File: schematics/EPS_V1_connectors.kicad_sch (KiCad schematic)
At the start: 14 parts, among them J1 Conn_01x19, J2 Conn_01x25, J3 Conn_01x9, J4 Conn_01x02, SW1 SWITCH, SW2 SWITCH, SW3 SWITCH

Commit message: Expose unregulated battery voltage for burn wire
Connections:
- net +12V: no longer J2.2 (Pin_2)
- net CHG_OUT: now also J2.2 (Pin_2)
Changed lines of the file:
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@@
 	)
 	(junction
-		(at 82.55 111.76)
-		(diameter 0)
-		(color 0 0 0 0)
-	)
-	(junction
 		(at 82.55 55.88)
 		(diameter 0)
@@
 	(wire
 		(pts
-			(xy 82.55 111.76) (xy 87.63 111.76)
-		)
-		(stroke
-			(width 0)
-			(type default)
-		)
-	)
-	(wire
-		(pts
 			(xy 82.55 58.42) (xy 82.55 60.96)
 		)
@@
 	(wire
 		(pts
-			(xy 82.55 111.76) (xy 82.55 114.3)
-		)
-		(stroke
-			(width 0)
-			(type default)
-		)
-	)
-	(wire
-		(pts
 			(xy 46.99 92.71) (xy 44.45 92.71)
 		)
@@
 	(wire
 		(pts
+			(xy 82.55 114.3) (xy 95.25 114.3)
+		)
+		(stroke
+			(width 0)
+			(type default)
+		)
+	)
+	(wire
+		(pts
 			(xy 46.99 97.79) (xy 44.45 97.79)
 		)
@@
 		)
 	)
+	(global_label "CHG_OUT"
+		(shape passive)
+		(at 82.55 111.76 0)
+		(fields_autoplaced yes)
+		(effects
+			(font
+				(size 1.27 1.27)
+			)
+			(justify left)
+		)
+		(property "Intersheetrefs" "${INTERSHEET_REFS}"
+			(at 92.8906 111.76 0)
+			(hide yes)
+			(show_name no)
+			(do_not_autoplace no)
+			(effects
+				(font
+					(size 1.27 1.27)
+				)
+				(justify left)
+			)
+		)
+	)
 	(global_label "I2C3_SDA"
 		(shape bidirectional)
@@
 	)
 	(symbol
-		(lib_id "power:+12V")
-		(at 87.63 111.76 0)
+		(lib_id "Device:D_Schottky")
+		(at 195.58 64.77 180)
 		(unit 1)
 		(body_style 1)
@@
 		(dnp no)
 		(fields_autoplaced yes)
-		(property "Reference" "#PWR016"
-			(at 87.63 115.57 0)
-			(hide yes)
+		(property "Reference" "D1"
+			(at 195.8975 58.42 0)
 			(show_name no)
 			(do_not_autoplace no)
@@
 			)
 		)
-		(property "Value" "+12V"
-			(at 87.63 106.68 0)
+		(property "Value" "D_Schottky"
+			(at 195.8975 60.96 0)
 			(show_name no)
 			(do_not_autoplace no)
@@
 			)
 		)
-		(property "Footprint" ""
-			(at 87.63 111.76 0)
+		(property "Footprint" "Diode_SMD:D_SOD-128"
+			(at 195.58 64.77 0)
 			(hide yes)
 			(show_name no)
@@
 		)
 		(property "Datasheet" ""
-			(at 87.63 111.76 0)
+			(at 195.58 64.77 0)
 			(hide yes)
 			(show_name no)
@@
 			)
 		)
-		(property "Description" "Power symbol creates a global label with name \"+12V\""
-			(at 87.63 111.76 0)
+		(property "Description" "Schottky diode"
+			(at 195.58 64.77 0)
 			(hide yes)
 			(show_name no)
@@
 			)
 		)
+		(property "MPN" "RSX301LAM30TR"
+			(at 195.58 64.77 0)
+			(hide yes)
+			(show_name no)
+			(do_not_autoplace no)
+			(effects
+				(font
+					(size 1.27 1.27)
+				)
+			)
+		)
+		(pin "2"
+		)
 		(pin "1"
 		)
@@
 			(project "EPS_V1"
 				(path "/85157432-5d03-48fa-ab40-27ed3d133f47/dccdebb8-bc98-4226-b239-70e380ba944d"
-					(reference "#PWR016")
+					(reference "D1")
 					(unit 1)
 				)
@@
 	)
 	(symbol
-		(lib_id "Device:D_Schottky")
-		(at 195.58 64.77 180)
+		(lib_id "Device:R_US")
+		(at 142.24 74.93 270)
 		(unit 1)
 		(body_style 1)
@@
 		(in_pos_files yes)
 		(dnp no)
-		(fields_autoplaced yes)
-		(property "Reference" "D1"
-			(at 195.8975 58.42 0)
+		(property "Reference" "R_ALRT1"
+			(at 145.796 72.644 90)
 			(show_name no)
 			(do_not_autoplace no)
@@
 					(size 1.27 1.27)
 				)
+				(justify right)
 			)
 		)
-		(property "Value" "D_Schottky"
-			(at 195.8975 60.96 0)
+		(property "Value" "1k"
+			(at 143.764 70.104 90)
 			(show_name no)
 			(do_not_autoplace no)
@@
 					(size 1.27 1.27)
 				)
+				(justify right)
 			)
 		)
-		(property "Footprint" "Diode_SMD:D_SOD-128"
-			(at 195.58 64.77 0)
+		(property "Footprint" "Resistor_SMD:R_0603_1608Metric"
+			(at 141.986 75.946 90)
 			(hide yes)
 			(show_name no)
@@
 		)
 		(property "Datasheet" ""
-			(at 195.58 64.77 0)
-			(hide yes)
-			(show_name no)
-			(do_not_autoplace no)
-			(effects
-				(font
-					(size 1.27 1.27)
-				)
-			)
-		)
-		(property "Description" "Schottky diode"
-			(at 195.58 64.77 0)
+			(at 142.24 74.93 0)
 			(hide yes)
 			(show_name no)
@@
 			)
 		)
-		(property "MPN" "RSX301LAM30TR"
-			(at 195.58 64.77 0)
+		(property "Description" "Resistor, US symbol"
+			(at 142.24 74.93 0)
 			(hide yes)
 			(show_name no)
@@
 			(project "EPS_V1"
 				(path "/85157432-5d03-48fa-ab40-27ed3d133f47/dccdebb8-bc98-4226-b239-70e380ba944d"
-					(reference "D1")
+					(reference "R_ALRT1")
 					(unit 1)
 				)
@@
 	)
 	(symbol
-		(lib_id "Device:R_US")
-		(at 142.24 74.93 270)
+		(lib_id "power:+12V")
+		(at 95.25 114.3 0)
 		(unit 1)
 		(body_style 1)
@@
 		(in_pos_files yes)
 		(dnp no)
-		(property "Reference" "R_ALRT1"
-			(at 145.796 72.644 90)
+		(fields_autoplaced yes)
+		(property "Reference" "#PWR016"
+			(at 95.25 118.11 0)
+			(hide yes)
 			(show_name no)
 			(do_not_autoplace no)
@@
 					(size 1.27 1.27)
 				)
-				(justify right)
 			)
 		)
-		(property "Value" "1k"
-			(at 143.764 70.104 90)
+		(property "Value" "+12V"
+			(at 95.25 109.22 0)
 			(show_name no)
 			(do_not_autoplace no)
@@
 					(size 1.27 1.27)
 				)
-				(justify right)
 			)
 		)
-		(property "Footprint" "Resistor_SMD:R_0603_1608Metric"
-			(at 141.986 75.946 90)
+		(property "Footprint" ""
+			(at 95.25 114.3 0)
 			(hide yes)
 			(show_name no)
@@
 		)
 		(property "Datasheet" ""
-			(at 142.24 74.93 0)
+			(at 95.25 114.3 0)
 			(hide yes)
 			(show_name no)
@@
 			)
 		)
-		(property "Description" "Resistor, US symbol"
-			(at 142.24 74.93 0)
+		(property "Description" "Power symbol creates a global label with name \"+12V\""
+			(at 95.25 114.3 0)
 			(hide yes)
 			(show_name no)
@@
 			)
 		)
-		(pin "2"
-		)
 		(pin "1"
 		)
@@
 			(project "EPS_V1"
 				(path "/85157432-5d03-48fa-ab40-27ed3d133f47/dccdebb8-bc98-4226-b239-70e380ba944d"
-					(reference "R_ALRT1")
+					(reference "#PWR016")
 					(unit 1)
 				)

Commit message: Switch out MP28167 for LTC3119 (MPPC buck-boost) in schematic
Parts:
- removed D_ALRT1: 4.7, Diode_SMD:D_0603_1608Metric, symbol Device:D_Zener
- added J5: Conn_01x01, Connector_PinHeader_2.54mm:PinHeader_1x01_P2.54mm_Horizontal, symbol Connector_Generic:Conn_01x01
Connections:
- new net CHG_IN: J5.1 (Pin_1)
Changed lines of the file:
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@@
-	)
-	(junction
-		(at 146.05 74.93)
-		(diameter 0)
-		(color 0 0 0 0)
 	)
 	(junction
@@
 	(wire
 		(pts
+			(xy 124.46 95.25) (xy 121.92 95.25)
+		)
+		(stroke
+			(width 0)
+			(type default)
+		)
+	)
+	(wire
+		(pts
 			(xy 242.57 80.01) (xy 242.57 77.47)
 		)
@@
 		(property "Intersheetrefs" "${INTERSHEET_REFS}"
 			(at 137.386 80.01 0)
+			(hide yes)
+			(show_name no)
+			(do_not_autoplace no)
+			(effects
+				(font
+					(size 1.27 1.27)
+				)
+				(justify left)
+			)
+		)
+	)
+	(global_label "CHG_IN"
+		(shape input)
+		(at 124.46 95.25 0)
+		(fields_autoplaced yes)
+		(effects
+			(font
+				(size 1.27 1.27)
+			)
+			(justify left)
+		)
+		(property "Intersheetrefs" "${INTERSHEET_REFS}"
+			(at 134.2186 95.25 0)
 			(hide yes)
 			(show_name no)
@@
 	)
 	(symbol
-		(lib_id "Device:D_Zener")
-		(at 146.05 78.74 270)
-		(unit 1)
-		(body_style 1)
-		(exclude_from_sim no)
-		(in_bom yes)
-		(on_board yes)
-		(in_pos_files yes)
-		(dnp no)
-		(property "Reference" "D_ALRT1"
-			(at 148.082 77.978 90)
-			(show_name no)
-			(do_not_autoplace no)
-			(effects
-				(font
-					(size 1.27 1.27)
-				)
-				(justify left)
-			)
-		)
-		(property "Value" "4.7"
-			(at 148.082 80.518 90)
-			(show_name no)
-			(do_not_autoplace no)
-			(effects
-				(font
-					(size 1.27 1.27)
-				)
-				(justify left)
-			)
-		)
-		(property "Footprint" "Diode_SMD:D_0603_1608Metric"
-			(at 146.05 78.74 0)
-			(hide yes)
-			(show_name no)
-			(do_not_autoplace no)
-			(effects
-				(font
-					(size 1.27 1.27)
-				)
-			)
-		)
-		(property "Datasheet" ""
-			(at 146.05 78.74 0)
-			(hide yes)
-			(show_name no)
-			(do_not_autoplace no)
-			(effects
-				(font
-					(size 1.27 1.27)
-				)
-			)
-		)
-		(property "Description" "Zener diode"
-			(at 146.05 78.74 0)
-			(hide yes)
-			(show_name no)
-			(do_not_autoplace no)
-			(effects
-				(font
-					(size 1.27 1.27)
-				)
-			)
-		)
-		(property "MPN" "TVSL02V05C005 (check)"
-			(at 146.05 78.74 90)
-			(hide yes)
-			(show_name no)
-			(do_not_autoplace no)
-			(effects
-				(font
-					(size 1.27 1.27)
-				)
-			)
-		)
-		(pin "1"
-		)
-		(pin "2"
-		)
-		(instances
-			(project "EPS_V1"
-				(path "/85157432-5d03-48fa-ab40-27ed3d133f47/dccdebb8-bc98-4226-b239-70e380ba944d"
-					(reference "D_ALRT1")
-					(unit 1)
-				)
-			)
-		)
-	)
-	(symbol
 		(lib_id "oresat-misc:OMRON-D2F-L3-D-RIGHT")
 		(at 238.76 80.01 0)
@@
 				(path "/85157432-5d03-48fa-ab40-27ed3d133f47/dccdebb8-bc98-4226-b239-70e380ba944d"
 					(reference "D3")
+					(unit 1)
+				)
+			)
+		)
+	)
+	(symbol
+		(lib_id "Connector_Generic:Conn_01x01")
+		(at 116.84 95.25 180)
+		(unit 1)
+		(body_style 1)
+		(exclude_from_sim no)
+		(in_bom yes)
+		(on_board yes)
+		(in_pos_files yes)
+		(dnp no)
+		(fields_autoplaced yes)
+		(property "Reference" "J5"
+			(at 116.84 88.9 0)
+			(show_name no)
+			(do_not_autoplace no)
+			(effects
+				(font
+					(size 1.27 1.27)
+				)
+			)
+		)
+		(property "Value" "Conn_01x01"
+			(at 116.84 91.44 0)
+			(show_name no)
+			(do_not_autoplace no)
+			(effects
+				(font
+					(size 1.27 1.27)
+				)
+			)
+		)
+		(property "Footprint" "Connector_PinHeader_2.54mm:PinHeader_1x01_P2.54mm_Horizontal"
+			(at 116.84 95.25 0)
+			(hide yes)
+			(show_name no)
+			(do_not_autoplace no)
+			(effects
+				(font
+					(size 1.27 1.27)
+				)
+			)
+		)
+		(property "Datasheet" ""
+			(at 116.84 95.25 0)
+			(hide yes)
+			(show_name no)
+			(do_not_autoplace no)
+			(effects
+				(font
+					(size 1.27 1.27)
+				)
+			)
+		)
+		(property "Description" "Generic connector, single row, 01x01, script generated (kicad-library-utils/schlib/autogen/connector/)"
+			(at 116.84 95.25 0)
+			(hide yes)
+			(show_name no)
+			(do_not_autoplace no)
+			(effects
+				(font
+					(size 1.27 1.27)
+				)
+			)
+		)
+		(pin "1"
+		)
+		(instances
+			(project "EPS_V1"
+				(path "/85157432-5d03-48fa-ab40-27ed3d133f47/dccdebb8-bc98-4226-b239-70e380ba944d"
+					(reference "J5")
 					(unit 1)
 				)
@@
 					(unit 1)
 				)
-			)
-		)
-	)
-	(symbol
-		(lib_id "power:GND")
-		(at 146.05 82.55 0)
-		(unit 1)
-		(body_style 1)
-		(exclude_from_sim no)
-		(in_bom yes)
-		(on_board yes)
-		(in_pos_files yes)
-		(dnp no)
-		(property "Reference" "#PWR0128"
-			(at 146.05 88.9 0)
-			(hide yes)
-			(show_name no)
-			(do_not_autoplace no)
-			(effects
-				(font
-					(size 1.27 1.27)
-				)
-			)
-		)
-		(property "Value" "GND"
-			(at 146.05 86.614 0)
-			(show_name no)
-			(do_not_autoplace no)
-			(effects
-				(font
-					(size 1.27 1.27)
-				)
-			)
-		)
-		(property "Footprint" ""
-			(at 146.05 82.55 0)
-			(hide yes)
-			(show_name no)
-			(do_not_autoplace no)
-			(effects
-				(font
-					(size 1.27 1.27)
-				)
-			)
-		)
-		(property "Datasheet" ""
-			(at 146.05 82.55 0)
-			(hide yes)
-			(show_name no)
-			(do_not_autoplace no)
-			(effects
-				(font
-					(size 1.27 1.27)
-				)
-			)
-		)
-		(property "Description" "Power symbol creates a global label with name \"GND\" , ground"
-			(at 146.05 82.55 0)
-			(hide yes)
-			(show_name no)
-			(do_not_autoplace no)
-			(effects
-				(font
-					(size 1.27 1.27)
-				)
-			)
-		)
-		(pin "1"
-		)
-		(instances
-			(project "EPS_V1"
-				(path "/85157432-5d03-48fa-ab40-27ed3d133f47/dccdebb8-bc98-4226-b239-70e380ba944d"
-					(reference "#PWR0128")
-					(unit 1)
-				)

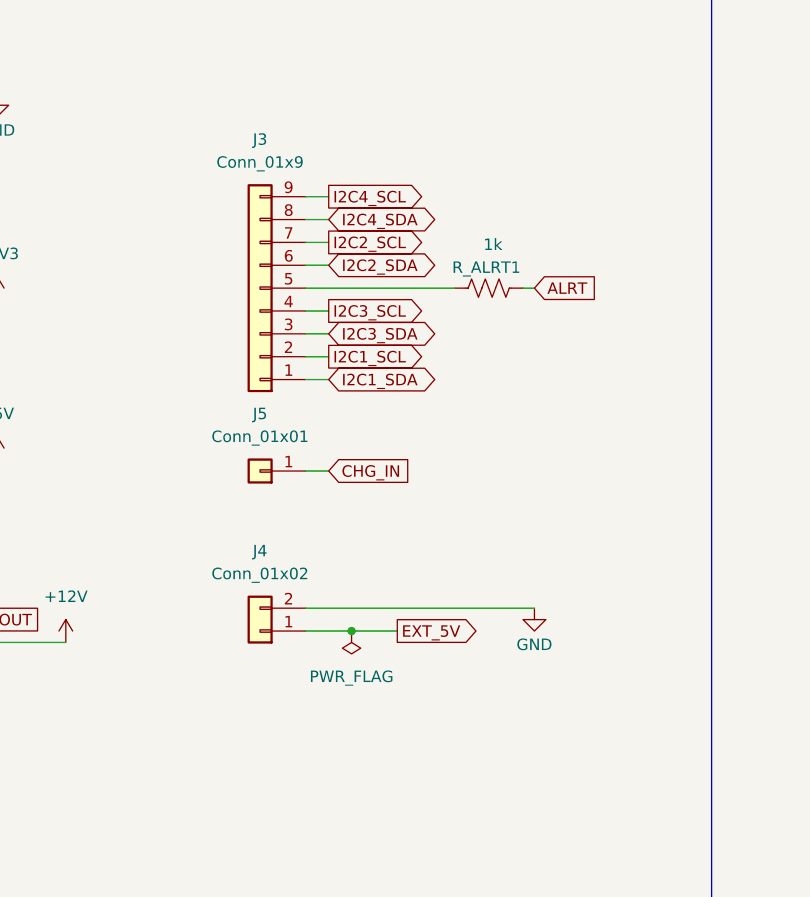
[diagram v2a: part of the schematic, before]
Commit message: Restore EPS layout + connector changes (recovered from local snapshot)
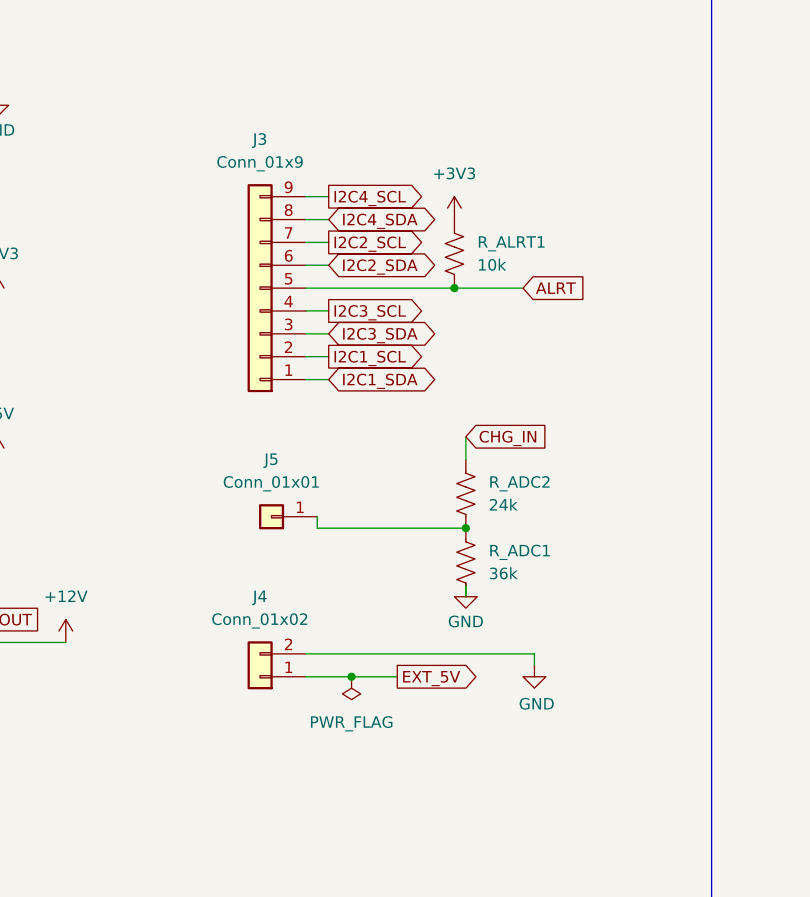
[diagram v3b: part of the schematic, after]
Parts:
- added R_ADC1: 36k, Resistor_SMD:R_0603_1608Metric, symbol Device:R_US
- added R_ADC2: 24k, Resistor_SMD:R_0603_1608Metric, symbol Device:R_US
- R_ALRT1: value 1k -> 10k
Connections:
- net +3V3: now also R_ALRT1.1
- net ALRT: now also J3.5 (Pin_5), R_ALRT1.2; no longer R_ALRT1.1
- net CHG_IN: now also R_ADC2.1; no longer J5.1 (Pin_1)
- net GND: now also R_ADC1.2
- new net: J5.1 (Pin_1), R_ADC1.1, R_ADC2.2
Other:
- moved on the sheet: J4, J5
